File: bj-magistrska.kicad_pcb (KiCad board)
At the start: 4 copper layers, 74.8 x 97 mm, 82 parts, among them J1 Screw_Terminal_01x02, J3 Screw_Terminal_01x02, J4 Conn_01x04, Q1 DMTH10H009LPSQ-13, SW1 VAL?, SW2 VAL?, SW3 RotaryEncoder_Switch_MP, U1 TSV732IS, U2 74LVC1G17, U3 TSV732IS, U4 NUCLEO144-H743ZI, U5 MCP1501-30xCH, U6 CR2013-MI2120

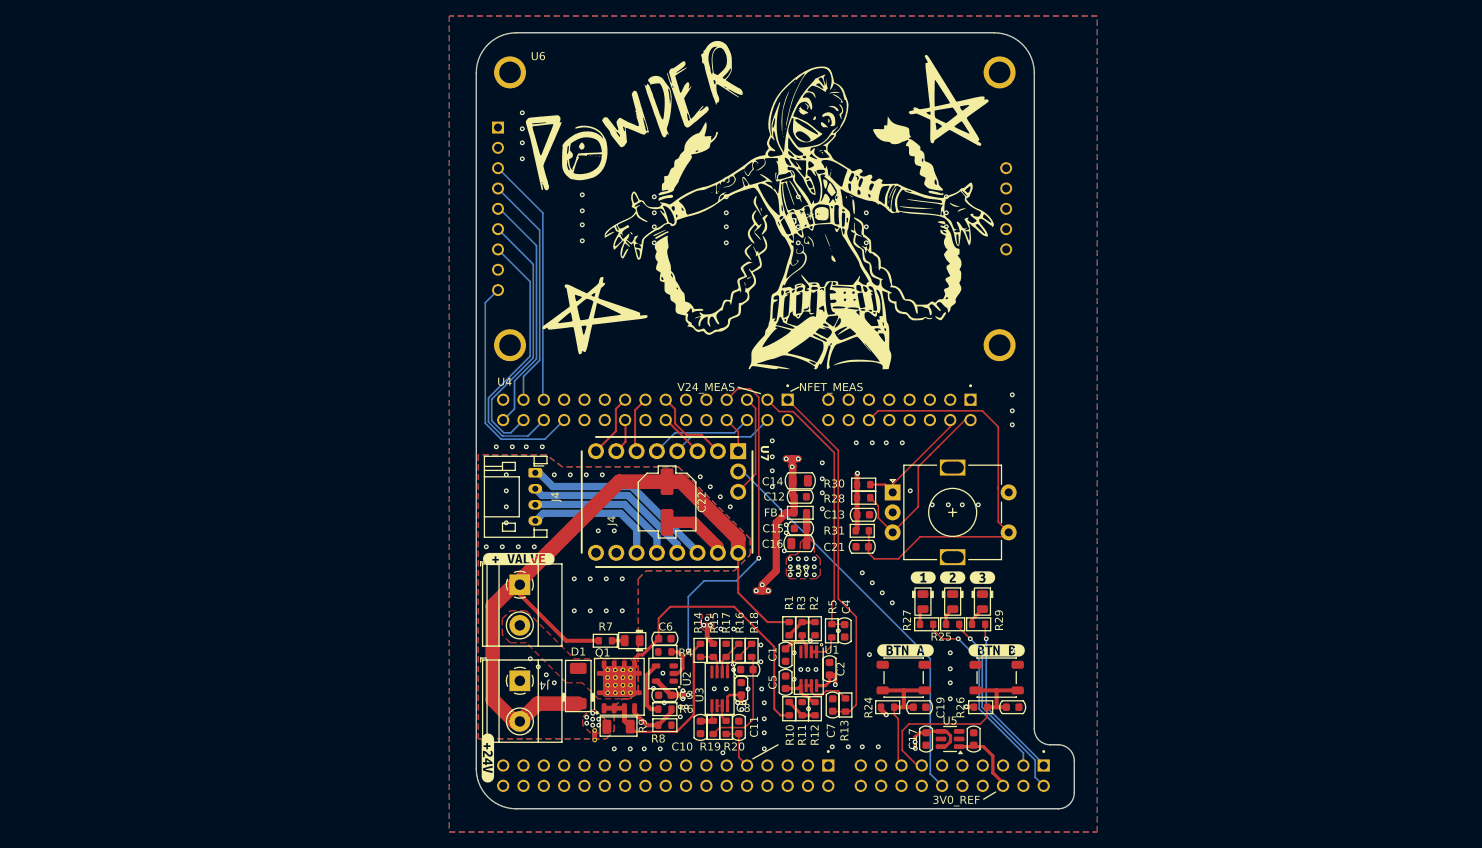
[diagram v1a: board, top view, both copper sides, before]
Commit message: Refactored Nucleo sheet. Added back my library. Started minor work on the PCB.
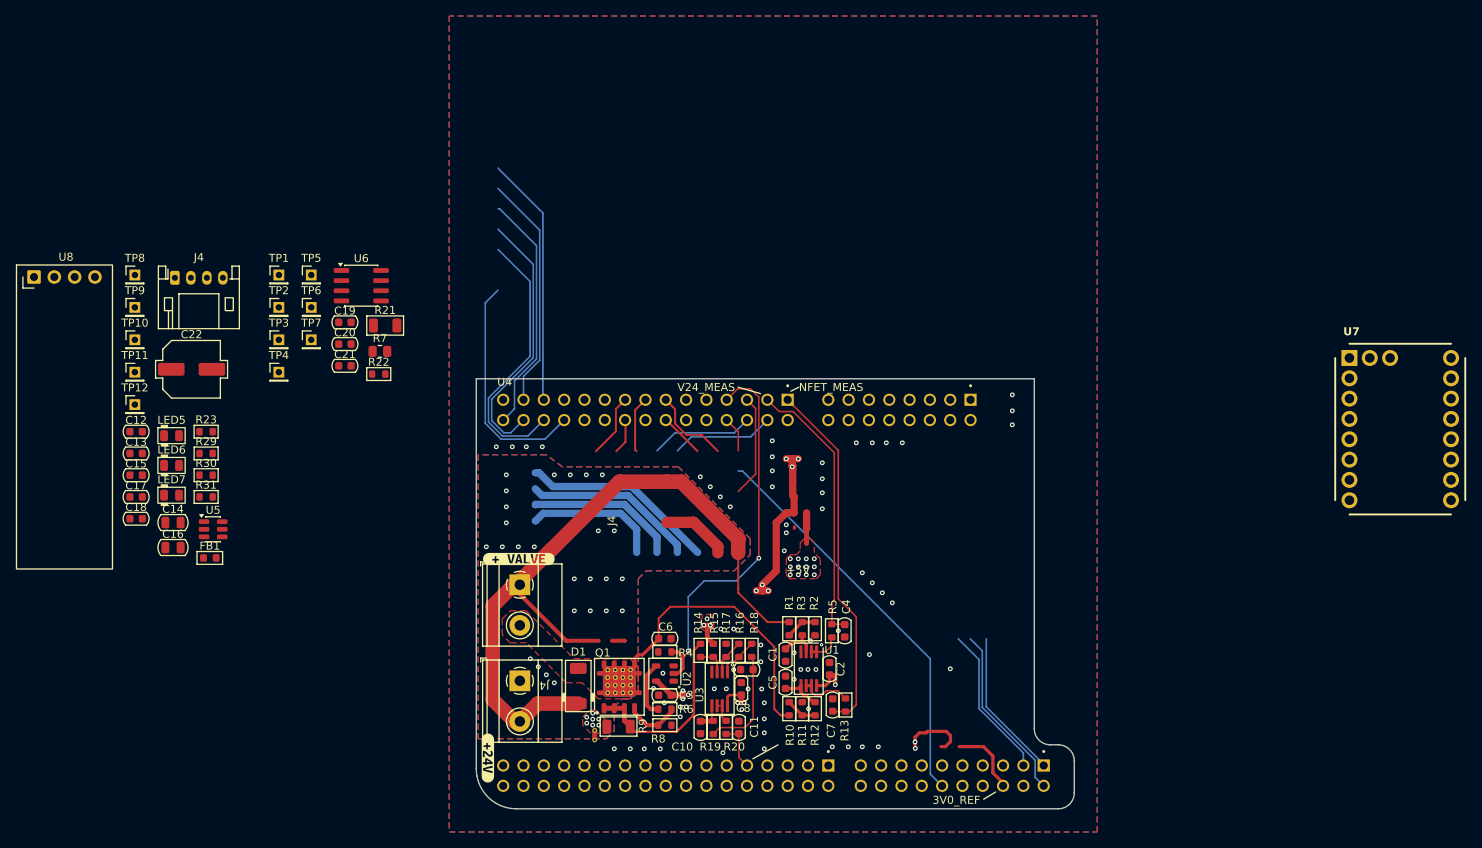
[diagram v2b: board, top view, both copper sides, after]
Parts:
- removed G*** (x4): LOGO, LOGO
- removed LED1: LED_0805_Red, PCM_LED_SMD_AKL:LED_0805_2012Metric
- removed LED3: GREEN, PCM_LED_SMD_AKL:LED_0805_2012Metric
- removed LED4: WHITE, PCM_LED_SMD_AKL:LED_0805_2012Metric
- removed R24, R26, R28: 10k, PCM_Resistor_SMD_AKL:R_0603_1608Metric
- removed R25, R27: 270R, PCM_Resistor_SMD_AKL:R_0603_1608Metric
- removed SW1, SW2: VAL?, athaniss-device:SW_SPST_PTS647_Sx70
- removed SW3: RotaryEncoder_Switch_MP, athaniss-device:RotaryEncoder_Alps_EC11E18244A5
- removed kibuzzard-66E6F459: G***, kibuzzard-66E6F459
- removed kibuzzard-66E6F464: G***, kibuzzard-66E6F464
- removed kibuzzard-66E6F48A: G***, kibuzzard-66E6F48A
- removed kibuzzard-66E6F497: G***, kibuzzard-66E6F497
- removed kibuzzard-66E6F4AB: G***, kibuzzard-66E6F4AB
- added LED6: ORANGE, PCM_LED_SMD_AKL:LED_0805_2012Metric, F.Cu at (43.8, 105.5)
- added LED7: ORANGE, PCM_LED_SMD_AKL:LED_0805_2012Metric, F.Cu at (43.8, 109.2)
- added R21: 0.015R, PCM_Resistor_SMD_AKL:R_1206_3216Metric, F.Cu at (70.5, 88.0)
- added R22: 220R, PCM_Resistor_SMD_AKL:R_0603_1608Metric, F.Cu at (69.7, 94.1)
- added R23: 1k, PCM_Resistor_SMD_AKL:R_0603_1608Metric, F.Cu at (48.1, 101.3)
- added TP1: TestPoint, Connector_PinHeader_2.00mm:PinHeader_1x01_P2.00mm_Vertical, F.Cu at (57.2, 81.7)
- added TP10: TestPoint, Connector_PinHeader_2.00mm:PinHeader_1x01_P2.00mm_Vertical, F.Cu at (39.2, 89.8)
- added TP11: TestPoint, Connector_PinHeader_2.00mm:PinHeader_1x01_P2.00mm_Vertical, F.Cu at (39.2, 93.9)
- added TP12: TestPoint, Connector_PinHeader_2.00mm:PinHeader_1x01_P2.00mm_Vertical, F.Cu at (39.2, 97.9)
- added TP2: TestPoint, Connector_PinHeader_2.00mm:PinHeader_1x01_P2.00mm_Vertical, F.Cu at (57.2, 85.8)
- added TP3: TestPoint, Connector_PinHeader_2.00mm:PinHeader_1x01_P2.00mm_Vertical, F.Cu at (57.2, 89.8)
- added TP4: TestPoint, Connector_PinHeader_2.00mm:PinHeader_1x01_P2.00mm_Vertical, F.Cu at (57.2, 93.9)
- added TP5: TestPoint, Connector_PinHeader_2.00mm:PinHeader_1x01_P2.00mm_Vertical, F.Cu at (61.2, 81.7)
- added TP6: TestPoint, Connector_PinHeader_2.00mm:PinHeader_1x01_P2.00mm_Vertical, F.Cu at (61.2, 85.8)
- added TP7: TestPoint, Connector_PinHeader_2.00mm:PinHeader_1x01_P2.00mm_Vertical, F.Cu at (61.2, 89.8)
- added TP8: TestPoint, Connector_PinHeader_2.00mm:PinHeader_1x01_P2.00mm_Vertical, F.Cu at (39.2, 81.7)
- added TP9: TestPoint, Connector_PinHeader_2.00mm:PinHeader_1x01_P2.00mm_Vertical, F.Cu at (39.2, 85.8)
- added U8: ER_OLEDM0.91_1x-I2C, Display:ER_OLEDM0.91_1x-I2C, F.Cu at (26.6, 82.0)
- C1, C5: value 100n -> 10n
- C21: value 100n -> 0
- C22: footprint PCM_Capacitor_SMD_AKL:C_Elec_6.3x7.7 -> PCM_Capacitor_SMD_AKL:C_Elec_6.3x5.8
- R30, R31: value 10k -> 270R
- R7: value 4k7 -> R; footprint PCM_Resistor_SMD_AKL:R_0603_1608Metric -> Resistor_SMD:R_0805_2012Metric
- U6: value CR2013-MI2120 -> INA240A2D; footprint Display:CR2013-MI2120 -> Package_SO:SOIC-8_3.9x4.9mm_P1.27mm
- moved C18 108.3 mm to (39.3, 112.2), turned to 0 degrees
- moved LED5 103.5 mm to (43.8, 101.8), turned to 0 degrees
- moved C17 103.3 mm to (39.3, 109.5), turned to 0 degrees
- moved R29 98.9 mm to (48.1, 104.0), turned to 0 degrees
- moved U5 95.8 mm to (49.0, 113.5), turned to 0 degrees
- moved C20 95.0 mm to (65.4, 90.4)
- moved U7 92.1 mm to (197.3, 101.0), turned to 0 degrees
- moved C13 91.2 mm to (39.3, 104.0)
- moved C19 86.4 mm to (65.4, 87.6)
- moved C12 83.4 mm to (39.3, 101.3)
- moved C15 83.3 mm to (39.3, 106.8), turned to 0 degrees
- moved R30 82.2 mm to (48.1, 106.8)
- moved R31 82.1 mm to (48.1, 109.5)
- moved C14 78.6 mm to (43.9, 112.7)
- moved C16 78.2 mm to (43.9, 115.8), turned to 0 degrees
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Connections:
- net TMC2209_CLK renamed Net-(U4-РЕ9)
- net TMC2209_DIAG renamed Net-(U4-РСЗ)
- net TMC2209_DIR renamed Net-(U4-PF2)
- net TMC2209_EN renamed Net-(U4-PD4)
- net TMC2209_MS1 renamed Net-(U7-MS1)
- net TMC2209_MS2 renamed Net-(U4-PE2)
- net TMC2209_RX renamed Net-(U4-PD6)
- net TMC2209_STEP renamed Net-(U4-РЕ5)
- net TMC2209_TX renamed Net-(U4-PD5)
- C11 pad 1: /Nucleo-144/I_MEAS -> /Output_Analog/MEAS_ILS
- C19 pad 1: /Nucleo-144/SW1 -> +5VA
- C20 pad 1: /Nucleo-144/SW2 -> /Output_Analog/MEAS_IHS
- C21 pad 1: /Nucleo-144/SW_ENC -> Net-(C21-Pad1)
- C21 pad 2: GND -> Net-(C21-Pad2)
- C4 pad 1: /Nucleo-144/V24_MEAS -> /Output_Analog/MEAS_VBUS
- C6 pad 1: /Output_Analog/LS1_RETURN -> /Output_Analog/COIL_IN
- C7 pad 1: /Nucleo-144/V_NFET_MEAS -> /Output_Analog/MEAS_VFET
- D1 pad 2: /Output_Analog/LS1_RETURN -> /Output_Analog/COIL_IN
- J3 pad 1: +12V -> /Output_Analog/COIL_OUT
- J3 pad 2: /Output_Analog/LS1_RETURN -> /Output_Analog/COIL_IN
- Q1 pad D: /Output_Analog/LS1_RETURN -> /Output_Analog/COIL_IN
- Q1 pad S: Net-(Q1-PadS) -> Net-(C21-Pad2)
- R10 pad 1: /Output_Analog/LS1_RETURN -> /Output_Analog/COIL_IN
- R13 pad 2: /Nucleo-144/V_NFET_MEAS -> /Output_Analog/MEAS_VFET
- R14 pad 1: Net-(Q1-PadS) -> Net-(C21-Pad2)
- R20 pad 2: /Nucleo-144/I_MEAS -> /Output_Analog/MEAS_ILS
- R29 pad 1: /Nucleo-144/LED_ORNG -> Net-(U4-PB15)
- R30 pad 1: +3V3 -> Net-(U4-PB8)
- R30 pad 2: /Nucleo-144/ENC_A -> Net-(LED6-A)
- R31 pad 1: +3V3 -> Net-(U4-PC6)
- R31 pad 2: /Nucleo-144/SW_ENC -> Net-(LED7-A)
- R5 pad 2: /Nucleo-144/V24_MEAS -> /Output_Analog/MEAS_VBUS
- R7 pad 1: +12V -> /Output_Analog/COIL_IN
- R7 pad 2: Net-(LED1-A) -> Net-(C21-Pad1)
- R9 pad 1: Net-(Q1-PadS) -> Net-(C21-Pad2)
- U4 pad CN7_1: /Nucleo-144/LED_ORNG -> Net-(U4-PC6)
- U4 pad CN7_13: /Nucleo-144/SW2 -> unconnected-(U4-PB5-PadCN7_13)
- U4 pad CN7_15: /Nucleo-144/SW1 -> unconnected-(U4-PB3-PadCN7_15)
- U4 pad CN7_2: /Nucleo-144/LED_GRN -> Net-(U4-PB8)
- U4 pad CN7_3: /Nucleo-144/LED_WHT -> Net-(U4-PB15)
- U4 pad CN8_12: /Nucleo-144/SW_ENC -> unconnected-(U4-PD2-PadCN8_12)
- U4 pad CN8_2: /Nucleo-144/ENC_B -> unconnected-(U4-PC8-PadCN8_2)
- U4 pad CN8_4: /Nucleo-144/ENC_A -> unconnected-(U4-PC9-PadCN8_4)
- U4 pad CN9_1: /Nucleo-144/V_NFET_MEAS -> unconnected-(U4-РАЗ-PadCN9_1)
- U4 pad CN9_24: ILI9341_SPI_MISO -> unconnected-(U4-PF8-PadCN9_24)
- U4 pad CN9_25: ILI9341_SPI_CS -> unconnected-(U4-PD0-PadCN9_25)
- U4 pad CN9_26: ILI9341_SPI_SCK -> unconnected-(U4-PF7-PadCN9_26)
- U4 pad CN9_27: ILI9341_RESET -> unconnected-(U4-PD1-PadCN9_27)
- U4 pad CN9_28: ILI9341_SPI_MOSI -> unconnected-(U4-PF9-PadCN9_28)
- U4 pad CN9_3: /Nucleo-144/V24_MEAS -> unconnected-(U4-PC0-PadCN9_3)
- U4 pad CN9_30: ILI9341_SPI_DC -> unconnected-(U4-PG1-PadCN9_30)
- U6 pad 1: +3V3 -> /Output_Analog/COIL_OUT
- U6 pad 3: ILI9341_SPI_CS -> GND
- U6 pad 4: ILI9341_RESET -> GND
- U6 pad 5: ILI9341_SPI_DC -> Net-(R22-Pad1)
- U6 pad 6: ILI9341_SPI_MOSI -> +5VA
- U6 pad 7: ILI9341_SPI_SCK -> GND
- U6 pad 8: +3V3 -> +12V
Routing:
- net (no net): track 0.00 -> 80.9 mm
- net /Nucleo-144/SW_ENC: track 53.2 -> 0.00 mm
- net /Nucleo-144/V_NFET_MEAS: track 45.0 -> 0.00 mm
- net /Output_Analog/LS1_RETURN: track 37.8 -> 0.00 mm
- net /Output_Analog/COIL_IN: track 0.00 -> 37.8 mm
- net /Nucleo-144/V24_MEAS: track 34.3 -> 0.00 mm
- net unconnected-(U4-PF7-PadCN9_26): track 0.00 -> 33.8 mm
- net ILI9341_SPI_SCK: track 33.8 -> 0.00 mm
- net unconnected-(U4-PF9-PadCN9_28): track 0.00 -> 33.2 mm
- net ILI9341_SPI_MOSI: track 33.2 -> 0.00 mm
- net unconnected-(U4-PD0-PadCN9_25): track 0.00 -> 31.3 mm
- net ILI9341_SPI_CS: track 31.3 -> 0.00 mm
- net unconnected-(U4-PG1-PadCN9_30): track 0.00 -> 30.2 mm
- net ILI9341_SPI_DC: track 30.2 -> 0.00 mm
- net unconnected-(U4-PD1-PadCN9_27): track 0.00 -> 29.4 mm
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- added copper zone on F.Cu, net /Output_Analog/COIL_IN
- removed copper zone on F.Cu, net /Output_Analog/LS1_RETURN
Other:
- board size 74.8 x 97 mm -> 74.8 x 53.7 mm

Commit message: Finalized V1.1. Refactor schematics (PCB is ripped up) for HS measurement. Kept LS custom chain for reference.
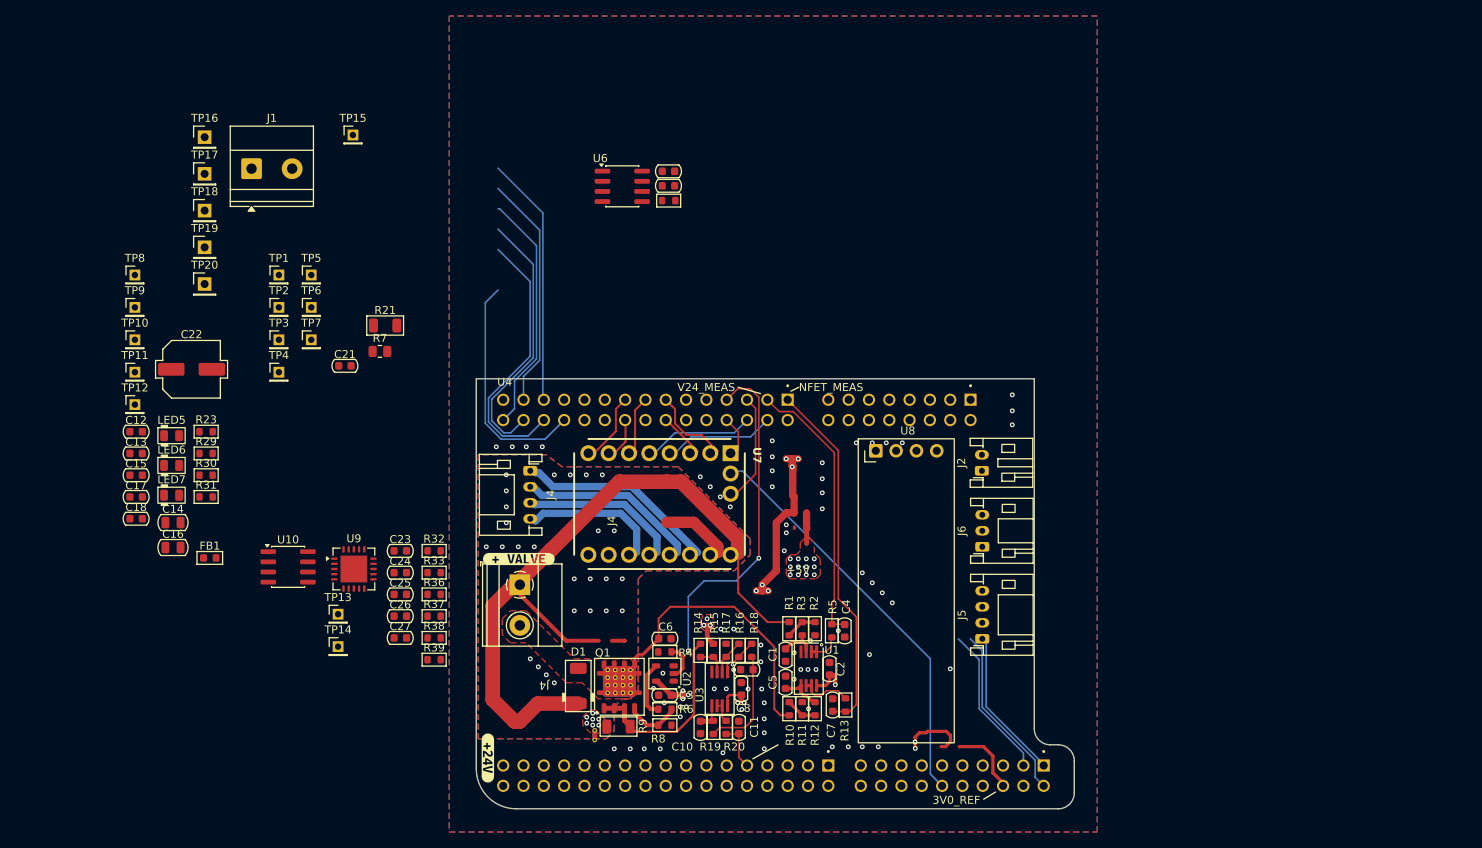
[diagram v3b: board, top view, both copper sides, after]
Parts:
- removed U5: MCP1501-30xCH, Package_TO_SOT_SMD:SOT-23-6
- added C23: 100n, PCM_Capacitor_SMD_AKL:C_0603_1608Metric, F.Cu at (72.3, 116.2)
- added C24: 100n, PCM_Capacitor_SMD_AKL:C_0603_1608Metric, F.Cu at (72.3, 118.9)
- added C25: 100n, PCM_Capacitor_SMD_AKL:C_0603_1608Metric, F.Cu at (72.3, 121.7)
- added C26: u1, PCM_Capacitor_SMD_AKL:C_0603_1608Metric, F.Cu at (72.3, 124.4)
- added C27: 10n, PCM_Capacitor_SMD_AKL:C_0603_1608Metric, F.Cu at (72.3, 127.1)
- added J2: Conn_01x02, Connector_JST:JST_PH_S2B-PH-K_1x02_P2.00mm_Horizontal, F.Cu at (145.1, 106.2)
- added J5: Conn_01x04, Connector_JST:JST_PH_S4B-PH-K_1x04_P2.00mm_Horizontal, F.Cu at (145.1, 127.2)
- added J6: Conn_01x03, Connector_JST:JST_PH_S3B-PH-K_1x03_P2.00mm_Horizontal, F.Cu at (145.1, 115.7)
- added R32: 270R, PCM_Resistor_SMD_AKL:R_0603_1608Metric, F.Cu at (76.6, 116.2)
- added R33: 270R, PCM_Resistor_SMD_AKL:R_0603_1608Metric, F.Cu at (76.6, 118.9)
- added R36: 1k, PCM_Resistor_SMD_AKL:R_0603_1608Metric, F.Cu at (76.6, 121.7)
- added R37: 10k, PCM_Resistor_SMD_AKL:R_0603_1608Metric, F.Cu at (76.6, 124.4)
- added R38: ~, PCM_Resistor_SMD_AKL:R_0603_1608Metric, F.Cu at (76.6, 127.1)
- added R39: ~, PCM_Resistor_SMD_AKL:R_0603_1608Metric, F.Cu at (76.6, 129.8)
- added TP13: TestPoint, Connector_PinHeader_2.00mm:PinHeader_1x01_P2.00mm_Vertical, F.Cu at (64.6, 124.1)
- added TP14: TestPoint, Connector_PinHeader_2.00mm:PinHeader_1x01_P2.00mm_Vertical, F.Cu at (64.6, 128.2)
- added TP15: TestPoint, Connector_PinHeader_2.00mm:PinHeader_1x01_P2.00mm_Vertical, F.Cu at (66.4, 64.2)
- added TP16: TestPoint, Connector_PinHeader_2.54mm:PinHeader_1x01_P2.54mm_Vertical, F.Cu at (47.9, 64.5)
- added TP17: TestPoint, Connector_PinHeader_2.54mm:PinHeader_1x01_P2.54mm_Vertical, F.Cu at (47.9, 69.1)
- added TP18: TestPoint, Connector_PinHeader_2.54mm:PinHeader_1x01_P2.54mm_Vertical, F.Cu at (47.9, 73.7)
- added TP19: TestPoint, Connector_PinHeader_2.54mm:PinHeader_1x01_P2.54mm_Vertical, F.Cu at (47.9, 78.3)
- added TP20: TestPoint, Connector_PinHeader_2.54mm:PinHeader_1x01_P2.54mm_Vertical, F.Cu at (47.9, 82.9)
- added U10: MCP1501-33xSN, Package_SO:SOIC-8_3.9x4.9mm_P1.27mm, F.Cu at (58.3, 118.2)
- added U9: MCP96xx01x-x-MX, Package_DFN_QFN:QFN-20-1EP_5x5mm_P0.65mm_EP3.35x3.35mm, F.Cu at (66.5, 118.5)
- C18: value 100n -> 1n
- R29, R30, R31: value 270R -> 560R
- moved U8 107.4 mm to (131.8, 103.7)
- moved U7 93.1 mm to (104.8, 110.3), turned to -90 degrees
- moved J1 72.3 mm to (53.8, 68.4), turned to 0 degrees
- moved J4 50.6 mm to (88.6, 106.2), turned to -90 degrees
- moved C20 45.0 mm to (105.9, 70.6), turned to 180 degrees
- moved C19 44.6 mm to (105.9, 68.8)
- moved R22 42.2 mm to (105.9, 72.4)
- moved U6 34.9 mm to (100.1, 70.6)
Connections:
- net /Nucleo-144/3V0_REF renamed ADC_VREF
- C11 pad 1: /Output_Analog/MEAS_ILS -> /Nucleo-144/ADC_IFET_LS
- C20 pad 1: /Output_Analog/MEAS_IHS -> /Nucleo-144/ADC_IFET_HS
- C4 pad 1: /Output_Analog/MEAS_VBUS -> /Nucleo-144/ADC_VBUS
- C7 pad 1: /Output_Analog/MEAS_VFET -> /Nucleo-144/ADC_VFET
- R13 pad 2: /Output_Analog/MEAS_VFET -> /Nucleo-144/ADC_VFET
- R20 pad 2: /Output_Analog/MEAS_ILS -> /Nucleo-144/ADC_IFET_LS
- R22 pad 2: /Output_Analog/MEAS_IHS -> /Nucleo-144/ADC_IFET_HS
- R29 pad 1: Net-(U4-PB15) -> Net-(U4-PA4)
- R30 pad 1: Net-(U4-PB8) -> Net-(U4-PD14)
- R31 pad 1: Net-(U4-PC6) -> Net-(U4-PB3)
- R5 pad 2: /Output_Analog/MEAS_VBUS -> /Nucleo-144/ADC_VBUS
- TP10 pad 1: Net-(U4-PB15) -> Net-(U4-PA4)
- TP2 pad 1: /Output_Analog/MEAS_IHS -> /Nucleo-144/ADC_IFET_HS
- TP3 pad 1: /Output_Analog/MEAS_ILS -> /Nucleo-144/ADC_IFET_LS
- TP4 pad 1: /Output_Analog/MEAS_VFET -> /Nucleo-144/ADC_VFET
- TP5 pad 1: /Output_Analog/MEAS_VBUS -> /Nucleo-144/ADC_VBUS
- TP8 pad 1: Net-(U4-PC6) -> Net-(U4-PB3)
- TP9 pad 1: Net-(U4-PB8) -> Net-(U4-PD14)
- U4 pad CN10_11: unconnected-(U4-PF6-PadCN10_11) -> /Nucleo-144/ADC_IFET_HS
- U4 pad CN10_9: /Nucleo-144/I_MEAS -> /Nucleo-144/ADC_IFET_LS
- U4 pad CN7_1: Net-(U4-PC6) -> unconnected-(U4-PC6-PadCN7_1)
- U4 pad CN7_11: unconnected-(U4-PC7-PadCN7_11) -> ENDSTOP_SW
- U4 pad CN7_15: unconnected-(U4-PB3-PadCN7_15) -> Net-(U4-PB3)
- U4 pad CN7_16: unconnected-(U4-PD14-PadCN7_16) -> Net-(U4-PD14)
- U4 pad CN7_17: unconnected-(U4-PA4-PadCN7_17) -> Net-(U4-PA4)
- U4 pad CN7_2: Net-(U4-PB8) -> I2C1_SCL
- U4 pad CN7_20: unconnected-(U4-PF3-PadCN7_20) -> /Nucleo-144/ADC_VFET
- U4 pad CN7_3: Net-(U4-PB15) -> unconnected-(U4-PB15-PadCN7_3)
- U4 pad CN7_4: unconnected-(U4-PB9-PadCN7_4) -> I2C1_SDA
- U4 pad CN9_3: unconnected-(U4-PC0-PadCN9_3) -> /Nucleo-144/ADC_VBUS
- U8 pad 1: unconnected-(U8-GND-Pad1) -> GND
- U8 pad 2: unconnected-(U8-VCC-Pad2) -> +3V3
- U8 pad 3: unconnected-(U8-SCL-Pad3) -> I2C1_SCL
- U8 pad 4: unconnected-(U8-SDA-Pad4) -> I2C1_SDA
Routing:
- net (no net): track 80.9 -> 1.61 mm
- net unconnected-(U4-РАЗ-PadCN9_1): track 0.00 -> 45.0 mm
- net /Nucleo-144/ADC_VBUS: track 0.00 -> 34.3 mm
- net Net-(U4-PB8): track 22.2 -> 0.00 mm
- net I2C1_SCL: track 0.00 -> 22.2 mm
- net unconnected-(U4-PB15-PadCN7_3): track 0.00 -> 19.8 mm
- net Net-(U4-PB15): track 19.8 -> 0.00 mm
- net unconnected-(U4-PC6-PadCN7_1): track 0.00 -> 19.2 mm
- net Net-(U4-PC6): track 19.2 -> 0.00 mm
- net /Nucleo-144/I_MEAS: track 6.03 -> 0.00 mm
- net /Nucleo-144/ADC_IFET_LS: track 0.00 -> 6.03 mm
- net unconnected-(U4-PB3-PadCN7_15): track 0.56 -> 0.00 mm
- net Net-(U4-PB3): track 0.00 -> 0.56 mm
